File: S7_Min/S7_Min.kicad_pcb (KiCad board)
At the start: 4 copper layers, 89 x 72 mm, 171 parts, among them J1 Barrel_Jack_Switch, J2 XILINX_JTAG, J3 HDMI_A, J4 Conn_02x15_Odd_Even, Q1 DMN2020L, Q2 DMN63D8LDW, Q3 DMN63D8LDW, Q4 DMN63D8LDW, Q5 DMN2020L, U1 TPS65581, U2 XC7S50-FTGB196, U3 REF3012, U4 QSPI_Flash_SOIC8, U5 MT47H128M16XX, U6 AZ1117-5.0, U7 TPD12S521, X1 DSC61XX

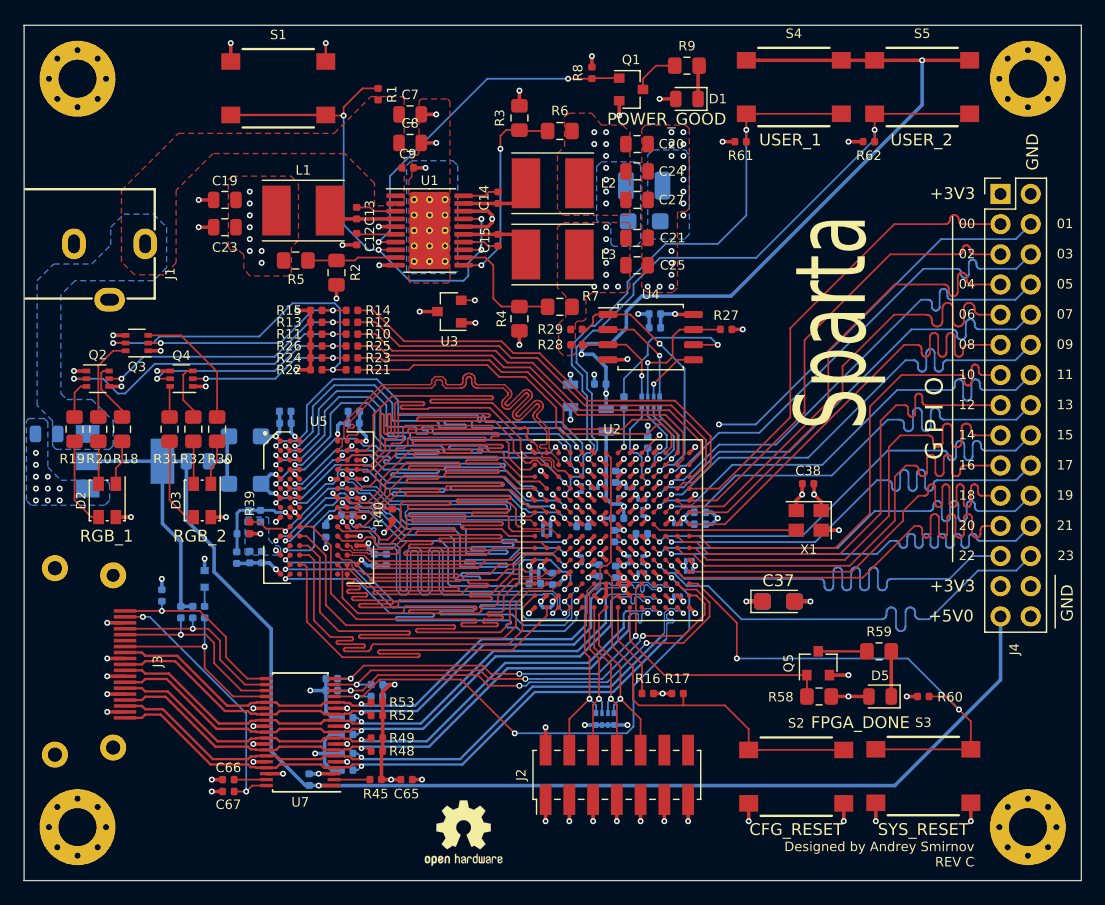
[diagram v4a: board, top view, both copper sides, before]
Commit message: Added gerbers for rev D main board and rev A ethernet board, schematic PDF for ethernet
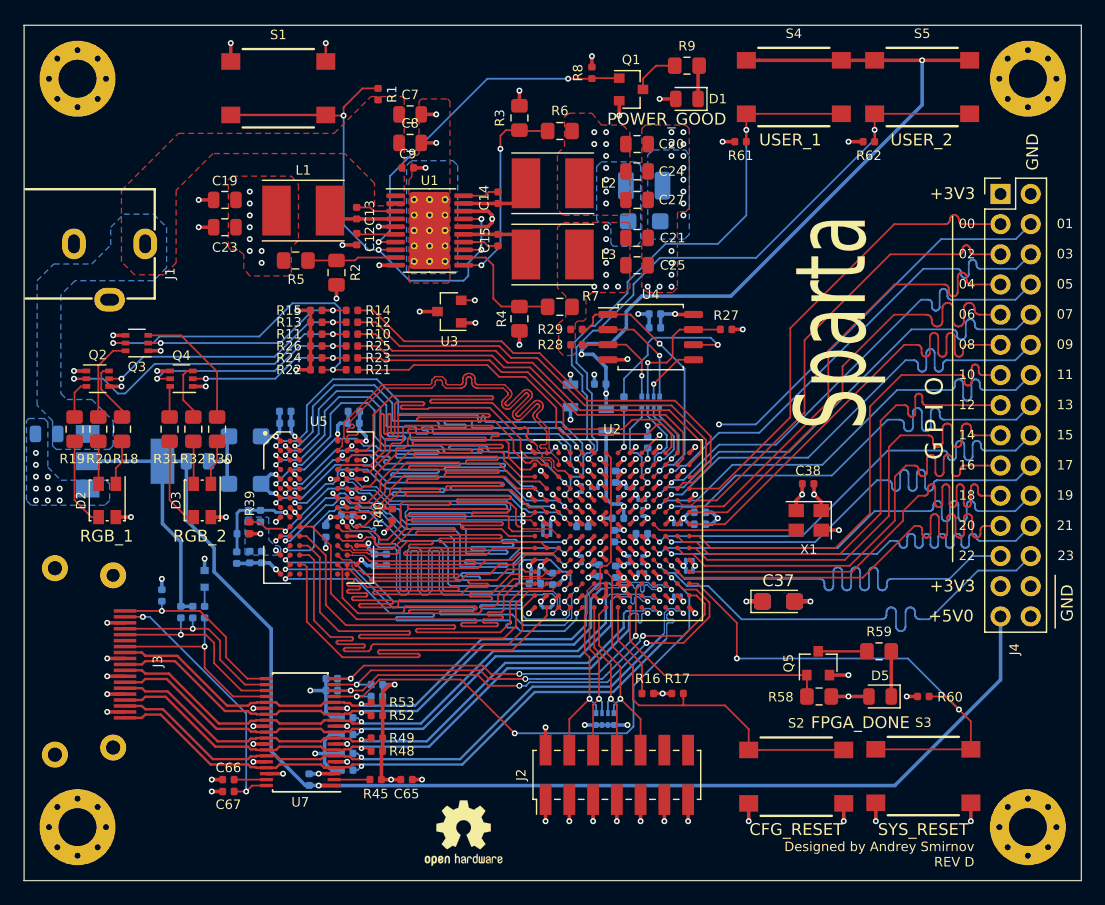
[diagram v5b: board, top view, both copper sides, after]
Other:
- board text added: "Designed by Andrey Smirnov REV D"
- board text removed: "Designed by Andrey Smirnov REV C"
